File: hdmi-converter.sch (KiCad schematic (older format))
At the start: 127 parts, among them J2 46756-1001, Q1 BSS138APW, Q2 BSS138APW, Q3 BSS138APW, Q4 BSS138APW, U2 LT9611, U3 TXB0104RUT, U4 NTS0102GT, Y2 ABM8G-24.000MHZ-18-D2Y-T

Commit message: Cleanup
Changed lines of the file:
@@
 $Descr A3 16535 11693
 encoding utf-8
-Sheet 3 13
+Sheet 3 12
 Title ""
 Date ""
@@
 	1    0    0    -1
 $EndComp
-Text GLabel 1375 5425 0    50   Input ~ 0
+Text GLabel 1175 5425 0    50   Input ~ 0
 DSI1_LN3_N
-Text GLabel 1375 5525 0    50   Input ~ 0
+Text GLabel 1175 5525 0    50   Input ~ 0
 DSI1_LN3_P
-Text GLabel 1375 5625 0    50   Input ~ 0
+Text GLabel 1175 5625 0    50   Input ~ 0
 DSI1_LN2_N
-Text GLabel 1375 5725 0    50   Input ~ 0
+Text GLabel 1175 5725 0    50   Input ~ 0
 DSI1_LN2_P
-Text GLabel 1375 5825 0    50   Input ~ 0
+Text GLabel 1175 5825 0    50   Input ~ 0
 DSI1_CLK_N
-Text GLabel 1375 5925 0    50   Input ~ 0
+Text GLabel 1175 5925 0    50   Input ~ 0
 DSI1_CLK_P
-Text GLabel 1375 6025 0    50   Input ~ 0
+Text GLabel 1175 6025 0    50   Input ~ 0
 DSI1_LN1_N
-Text GLabel 1375 6125 0    50   Input ~ 0
+Text GLabel 1175 6125 0    50   Input ~ 0
 DSI1_LN1_P
-Text GLabel 1375 6225 0    50   Input ~ 0
+Text GLabel 1175 6225 0    50   Input ~ 0
 DSI1_LN0_N
 $Comp
@@
 	1700 10500 1550 10500
 Wire Wire Line
-	2500 10500 2650 10500
+	2500 10500 3350 10500
 Wire Wire Line
-	2500 10100 2650 10100
+	2500 10100 3350 10100
 Wire Wire Line
-	2500 10300 2650 10300
+	2500 10300 3350 10300
 Wire Wire Line
-	2500 9900 2650 9900
+	2500 9900 3350 9900
 Wire Wire Line
 	2000 9400 2000 9500
@@
 Connection ~ 1425 5225
 Wire Wire Line
-	1425 5225 1375 5225
+	1425 5225 675  5225
 Text GLabel 925  775  0    50   Input ~ 0
 3V3_SYS
@@
 $EndComp
 Wire Wire Line
-	8875 7950 12425 7950
+	8550 7950 12425 7950
 $Comp
 L sa800u-baseboard-hw:GND #PWR036
@@
 Connection ~ 2025 5025
 Wire Wire Line
-	1375 5125 1725 5125
+	675  5125 1725 5125
 Wire Wire Line
 	1425 4425 1725 4425
 Wire Wire Line
-	1375 5025 2025 5025
+	675  5025 2025 5025
 Wire Wire Line
 	1725 4425 2025 4425
@@
 Text Label 7175 8075 2    50   ~ 0
 VCOM
-Text Label 8875 6400 0    50   ~ 0
+Text Label 8550 6400 0    50   ~ 0
 HDMI_TX_D2_P
-Text Label 8875 6500 0    50   ~ 0
+Text Label 8550 6500 0    50   ~ 0
 HDMI_TX_D2_N
-Text Label 8875 6800 0    50   ~ 0
+Text Label 8550 6800 0    50   ~ 0
 HDMI_TX_D1_N
-Text Label 8875 7100 0    50   ~ 0
+Text Label 8550 7100 0    50   ~ 0
 HDMI_TX_D0_N
-Text Label 8875 7400 0    50   ~ 0
+Text Label 8550 7400 0    50   ~ 0
 HDMI_TX_CLK_N
-Text Label 8875 6700 0    50   ~ 0
+Text Label 8550 6700 0    50   ~ 0
 HDMI_TX_D1_P
-Text Label 8875 7000 0    50   ~ 0
+Text Label 8550 7000 0    50   ~ 0
 HDMI_TX_D0_P
-Text Label 8875 7300 0    50   ~ 0
+Text Label 8550 7300 0    50   ~ 0
 HDMI_TX_CLK_P
-Text Label 6350 10175 2    50   ~ 0
+Text Label 6050 10175 0    50   ~ 0
 LT9611_CEC
 Wire Wire Line
-	8875 6400 11375 6400
+	8550 6400 11375 6400
 Wire Wire Line
-	8875 6500 11075 6500
+	8550 6500 11075 6500
 Wire Wire Line
-	8875 7000 10175 7000
+	8550 7000 10175 7000
 Wire Wire Line
-	8875 7100 9875 7100
+	8550 7100 9875 7100
 Wire Wire Line
-	8875 7400 9275 7400
+	8550 7400 9275 7400
 Wire Wire Line
-	8875 7300 9575 7300
+	8550 7300 9575 7300
 Wire Wire Line
-	8875 6800 10475 6800
+	8550 6800 10475 6800
 Wire Wire Line
-	8875 6700 10775 6700
+	8550 6700 10775 6700
 Wire Wire Line
 	1700 9700 1650 9700
@@
 Wire Wire Line
 	3050 9100 3300 9100
-Text Label 1375 6525 2    50   ~ 0
+Text Label 700  6525 0    50   ~ 0
 LT9611_I2S_WS
-Text Label 1375 6625 2    50   ~ 0
+Text Label 700  6625 0    50   ~ 0
 LT9611_I2S_SCLK
-Text Label 1375 6725 2    50   ~ 0
+Text Label 700  6725 0    50   ~ 0
 LT9611_I2S_MCLK
-Text Label 1375 6825 2    50   ~ 0
+Text Label 700  6825 0    50   ~ 0
 LT9611_I2S_D0_SPDIF
-Text Label 2650 9900 0    50   ~ 0
+Text Label 3350 9900 2    50   ~ 0
 LT9611_I2S_WS
-Text Label 2650 10100 0    50   ~ 0
+Text Label 3350 10100 2    50   ~ 0
 LT9611_I2S_SCLK
-Text Label 2650 10300 0    50   ~ 0
+Text Label 3350 10300 2    50   ~ 0
 LT9611_I2S_MCLK
-Text Label 2650 10500 0    50   ~ 0
+Text Label 3350 10500 2    50   ~ 0
 LT9611_I2S_D0_SPDIF
 Wire Wire Line
@@
 Connection ~ 5300 9750
 Wire Wire Line
-	5300 9750 5500 9750
+	5300 9750 6025 9750
 Wire Wire Line
 	5250 10575 5300 10575
@@
 Wire Wire Line
 	5300 10575 5425 10575
-Text Label 1375 5225 2    50   ~ 0
+Text Label 675  5225 0    50   ~ 0
 LT9611_RST_N
-Text Label 1375 4925 2    50   ~ 0
+Text Label 675  4925 0    50   ~ 0
 LT9611_INTO_GPIO5
 Wire Wire Line
@@
 	6550 10175 6600 10175
 Wire Wire Line
-	6350 10175 6550 10175
+	6050 10175 6550 10175
 Text GLabel 6650 9325 0    50   Input ~ 0
 3V3_SYS
@@
 Connection ~ 7050 10175
 Wire Wire Line
-	7050 10175 7250 10175
-Text Label 7250 10175 0    50   ~ 0
+	7050 10175 7675 10175
+Text Label 7675 10175 2    50   ~ 0
 HDMI_CEC
 Wire Wire Line
@@
 Connection ~ 5425 10575
 Wire Wire Line
-	5425 10575 5500 10575
+	5425 10575 6025 10575
 Text Notes 5750 10900 0    50   ~ 0
 Note:\nplace close to\npin 17 of U2
 Wire Wire Line
-	1375 5425 3500 5425
+	1175 5425 3500 5425
 Wire Wire Line
-	1375 5525 3500 5525
+	1175 5525 3500 5525
 Wire Wire Line
-	1375 5625 3500 5625
+	1175 5625 3500 5625
 Wire Wire Line
-	1375 5725 3500 5725
+	1175 5725 3500 5725
 Wire Wire Line
-	1375 5825 3500 5825
+	1175 5825 3500 5825
 Wire Wire Line
-	1375 5925 3500 5925
+	1175 5925 3500 5925
 Wire Wire Line
-	1375 6025 3500 6025
+	1175 6025 3500 6025
 Wire Wire Line
-	1375 6125 3500 6125
+	1175 6125 3500 6125
 Wire Wire Line
-	1375 6225 3500 6225
+	1175 6225 3500 6225
 Wire Wire Line
-	1375 6325 3500 6325
+	1175 6325 3500 6325
 Wire Wire Line
-	1375 6525 3500 6525
+	700  6525 3500 6525
 Wire Wire Line
-	1375 6625 3500 6625
+	700  6625 3500 6625
 Wire Wire Line
-	1375 6725 3500 6725
+	700  6725 3500 6725
 Wire Wire Line
-	1375 6825 3500 6825
+	700  6825 3500 6825
 Wire Wire Line
 	1375 7875 3500 7875
@@
 	0    1    1    0
 $EndComp
-Text Label 1375 5025 2    50   ~ 0
+Text Label 675  5025 0    50   ~ 0
 LT9611_SCL
-Text Label 1375 5125 2    50   ~ 0
+Text Label 675  5125 0    50   ~ 0
 LT9611_SDA
-Text Label 8875 7950 0    50   ~ 0
+Text Label 8550 7950 0    50   ~ 0
 VCOM
 Text GLabel 1550 9400 0    50   Input ~ 0
@@
 Wire Wire Line
 	4800 4925 5625 4925
-Text GLabel 1375 6325 0    50   Input ~ 0
+Text GLabel 1175 6325 0    50   Input ~ 0
 DSI1_LN0_P
 $Comp
@@
 Wire Wire Line
 	11625 2225 11625 3425
-Text Label 5500 10575 0    50   ~ 0
+Text Label 6025 10575 2    50   ~ 0
 LT9611_RST_N
-Text Label 5500 9750 0    50   ~ 0
+Text Label 6025 9750 2    50   ~ 0
 LT9611_INTO_GPIO5
 $Comp
@@
 	2025 5275 2025 5025
 Wire Wire Line
-	1375 4925 2350 4925
+	675  4925 2350 4925
 Wire Wire Line
 	2350 5275 2350 4925

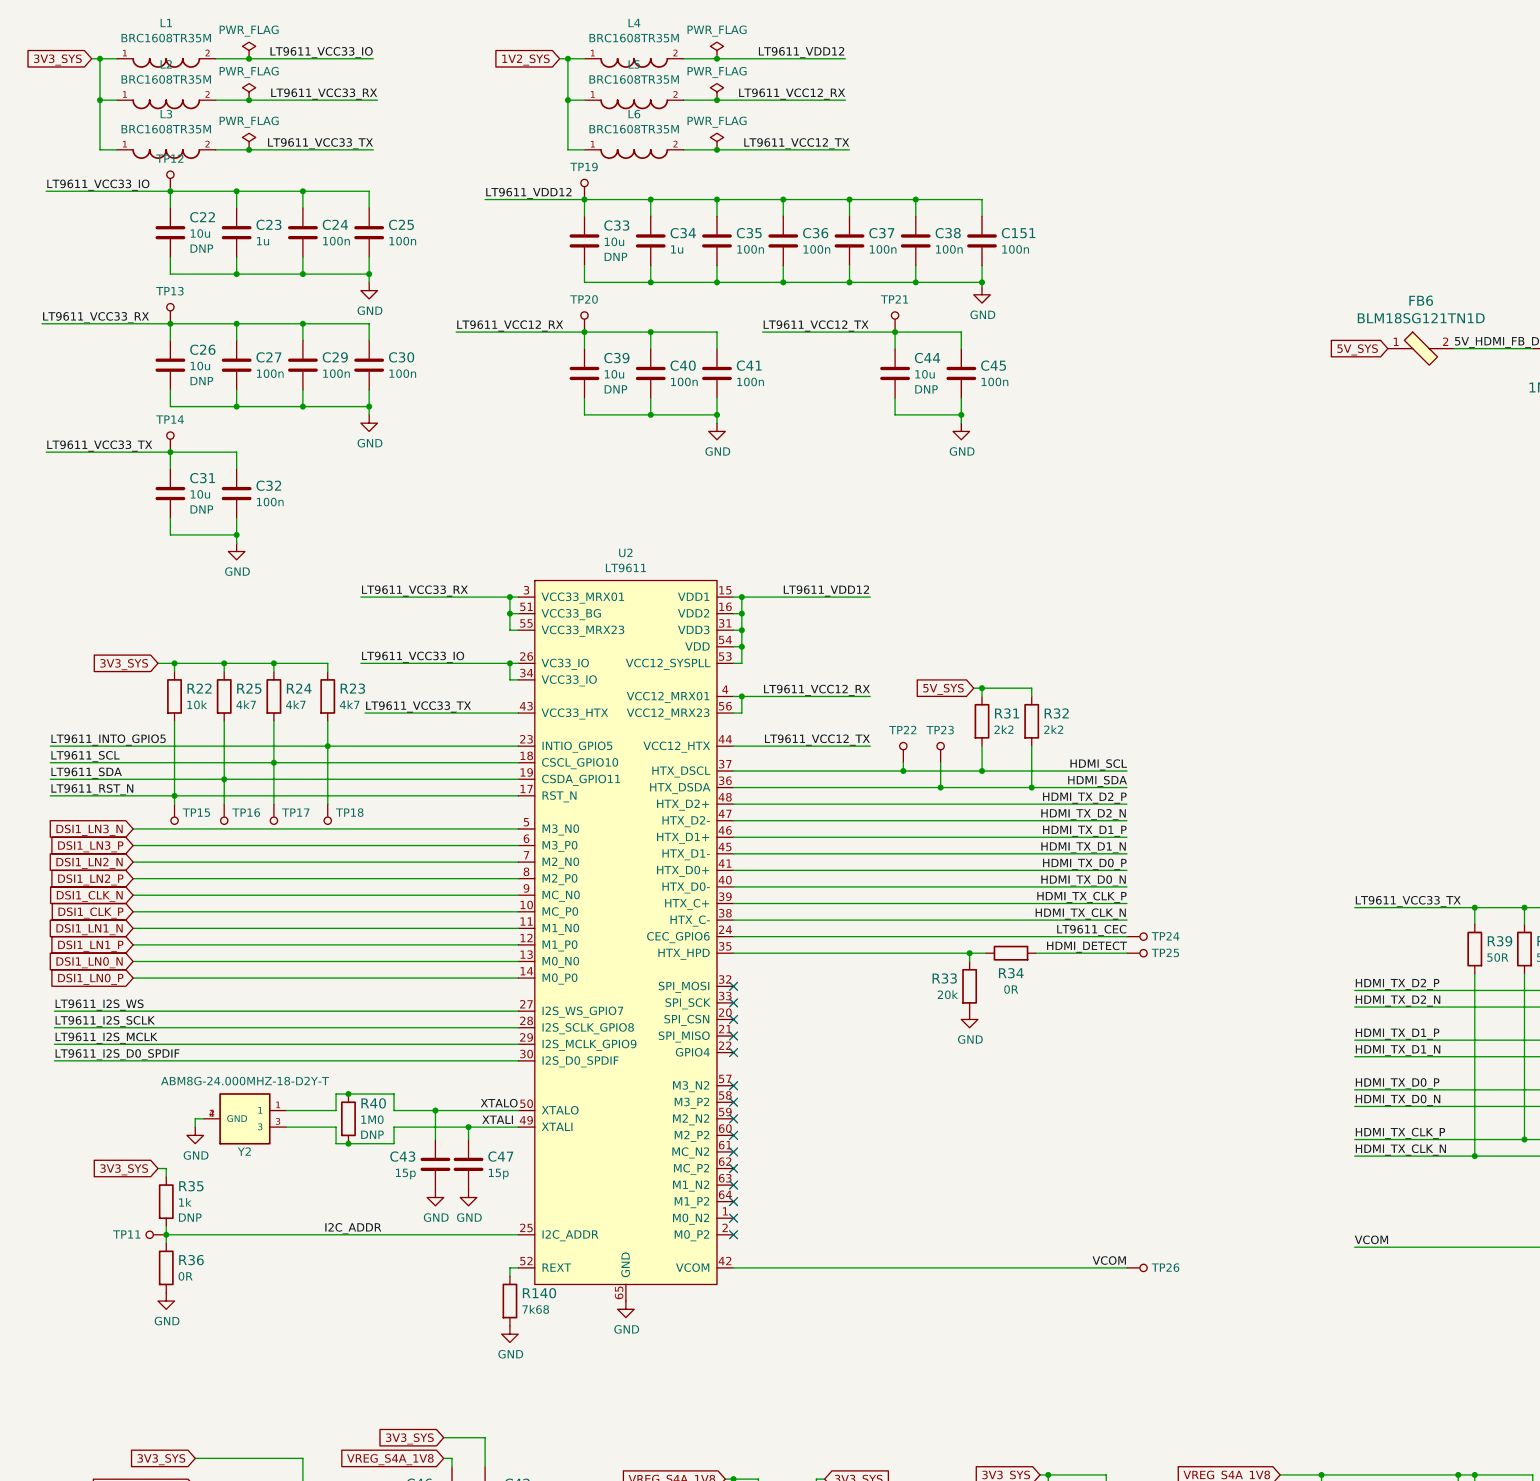
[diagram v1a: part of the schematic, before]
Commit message: Reorganize schematics, add descriptions in top left corner
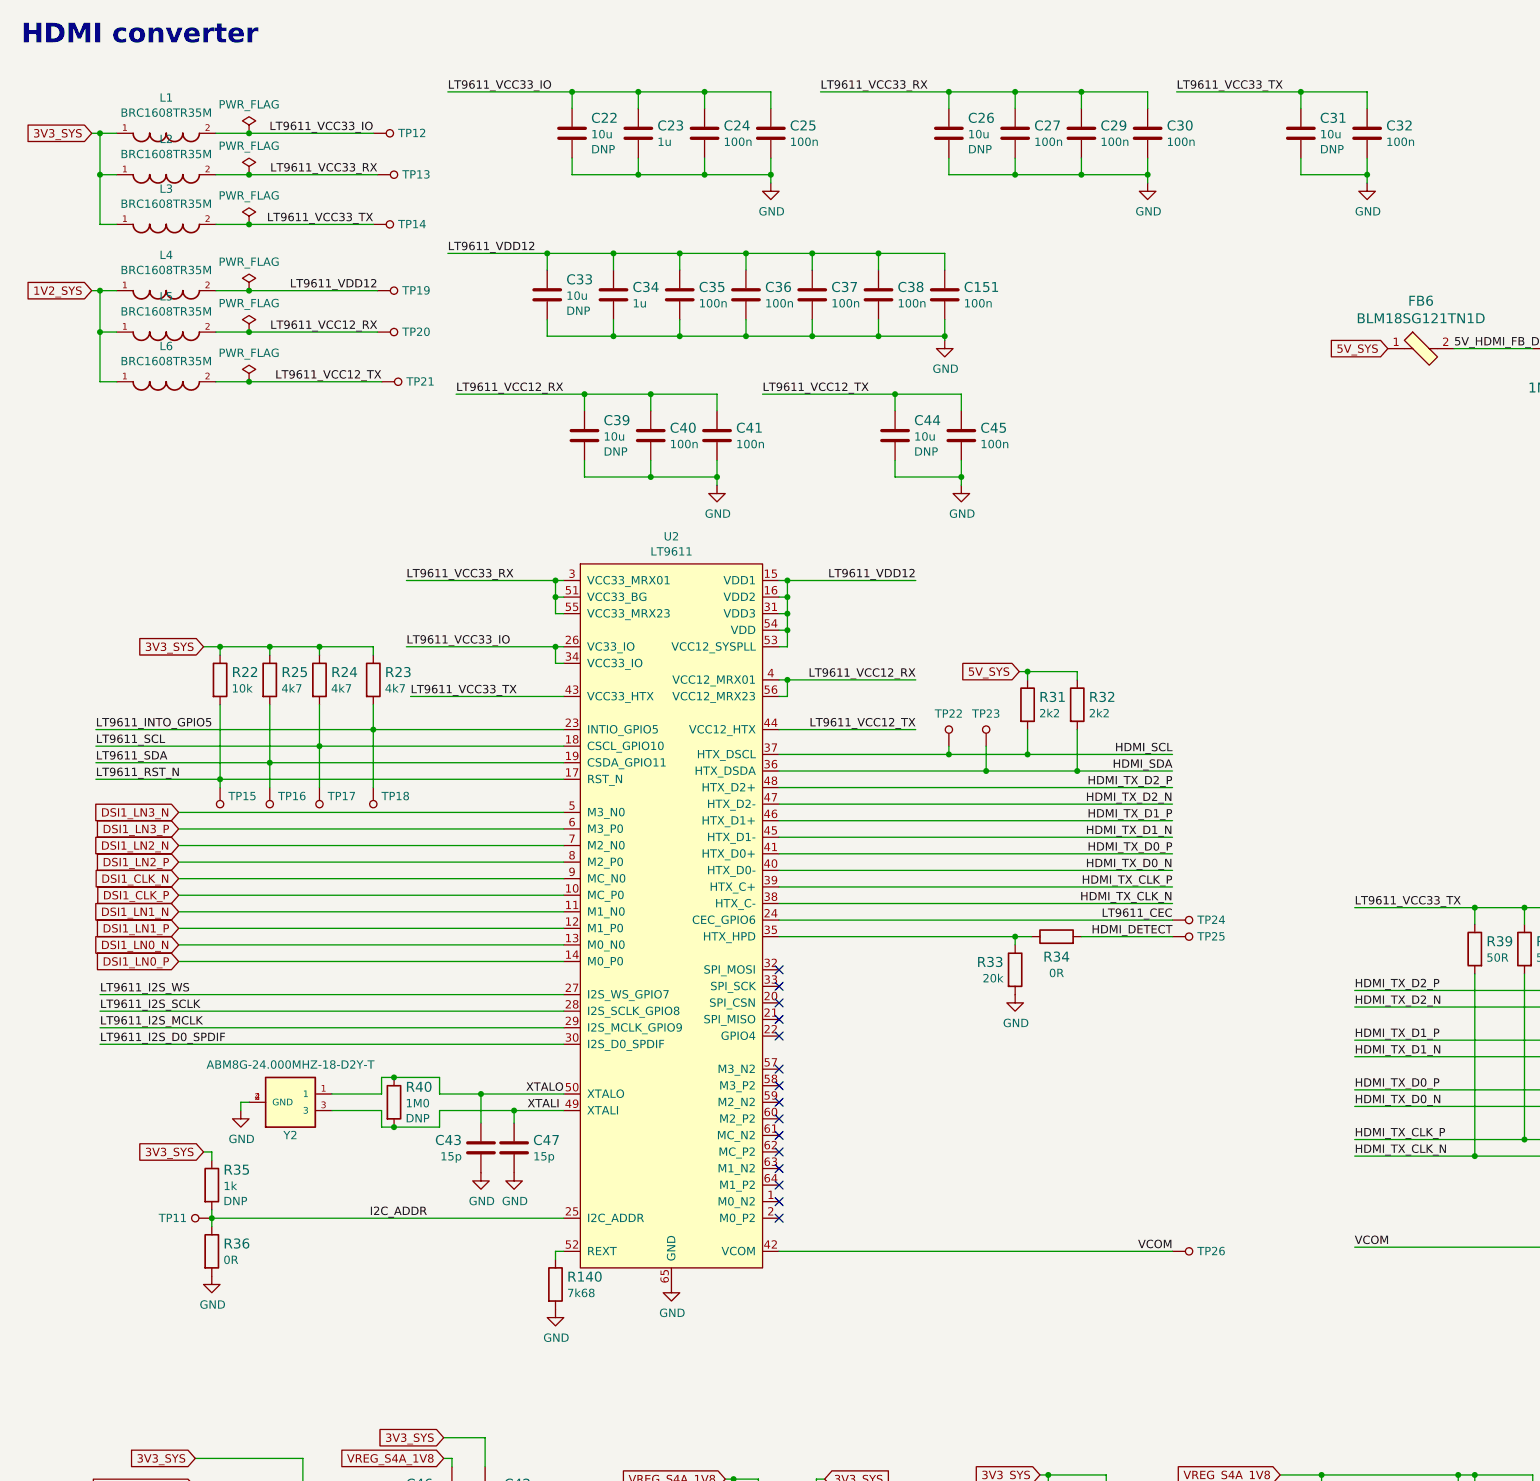
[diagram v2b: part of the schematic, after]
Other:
- note added: "HDMI converter"
- moved on the sheet: C151, C22, C23, C24, C25, C26, C27, C29, C30, C31, C32, C33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

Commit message: Add testpoints to PCB, udpate cache, connect STUSB4500 reset to SoM and pulldown with 10k
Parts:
- removed TP16, TP17: TP_SMD_0_75MM, sa800u-baseboard-hw-footprints:Testpoint_smd_0_75mm, symbol sa800u-baseboard-hw:TP_SMD_0_75MM
- added TP16: TP, antmicro-footprints:TP-R-1.5, symbol antmicroTestPoints:TP
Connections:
- net GND: now also TP16.1
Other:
- moved on the sheet: TP15, TP18
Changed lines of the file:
@@
 L sa800u-baseboard-hw:TP_SMD_0_75MM TP?
 U 1 1 6297FFC8
-P 1700 5275
+P 6125 10575
 AR Path="/618E716E/6297FFC8" Ref="TP?"  Part="1"
 AR Path="/6197686D/6297FFC8" Ref="TP15"  Part="1"
-F 0 "TP15" H 1750 5322 50  0000 L CNN
-F 1 "TP_SMD_0_75MM" H 1700 5175 50  0001 C CNN
-F 2 "sa800u-baseboard-hw-footprints:Testpoint_smd_0_75mm" H 1900 5475 60  0001 L CNN
-F 3 "" H 1900 5575 60  0001 L CNN
-	1    1700 5275
-	1    0    0    -1
-$EndComp
-$Comp
-L sa800u-baseboard-hw:TP_SMD_0_75MM TP?
-U 1 1 62A0D2B6
-P 2000 5275
-AR Path="/618E716E/62A0D2B6" Ref="TP?"  Part="1"
-AR Path="/6197686D/62A0D2B6" Ref="TP16"  Part="1"
-F 0 "TP16" H 2050 5322 50  0000 L CNN
-F 1 "TP_SMD_0_75MM" H 2000 5175 50  0001 C CNN
-F 2 "sa800u-baseboard-hw-footprints:Testpoint_smd_0_75mm" H 2200 5475 60  0001 L CNN
-F 3 "" H 2200 5575 60  0001 L CNN
-	1    2000 5275
-	1    0    0    -1
-$EndComp
-$Comp
-L sa800u-baseboard-hw:TP_SMD_0_75MM TP?
-U 1 1 62A99631
-P 2300 5275
-AR Path="/618E716E/62A99631" Ref="TP?"  Part="1"
-AR Path="/6197686D/62A99631" Ref="TP17"  Part="1"
-F 0 "TP17" H 2350 5322 50  0000 L CNN
-F 1 "TP_SMD_0_75MM" H 2300 5175 50  0001 C CNN
-F 2 "sa800u-baseboard-hw-footprints:Testpoint_smd_0_75mm" H 2500 5475 60  0001 L CNN
-F 3 "" H 2500 5575 60  0001 L CNN
-	1    2300 5275
-	1    0    0    -1
-$EndComp
-$Comp
-L sa800u-baseboard-hw:TP_SMD_0_75MM TP?
-U 1 1 62AE01B3
-P 2625 5275
-AR Path="/618E716E/62AE01B3" Ref="TP?"  Part="1"
-AR Path="/6197686D/62AE01B3" Ref="TP18"  Part="1"
-F 0 "TP18" H 2675 5322 50  0000 L CNN
-F 1 "TP_SMD_0_75MM" H 2625 5175 50  0001 C CNN
-F 2 "sa800u-baseboard-hw-footprints:Testpoint_smd_0_75mm" H 2825 5475 60  0001 L CNN
-F 3 "" H 2825 5575 60  0001 L CNN
-	1    2625 5275
-	1    0    0    -1
-$EndComp
-Wire Wire Line
-	1700 5175 1700 5125
-Wire Wire Line
-	2000 5175 2000 5025
-Wire Wire Line
-	2300 5175 2300 4925
+F 0 "TP15" V 6125 10525 50  0000 R CNN
+F 1 "TP_SMD_0_75MM" H 6125 10475 50  0001 C CNN
+F 2 "sa800u-baseboard-hw-footprints:Testpoint_smd_0_75mm" H 6325 10775 60  0001 L CNN
+F 3 "" H 6325 10875 60  0001 L CNN
+	1    6125 10575
+	0    -1   -1   0
+$EndComp
 Wire Wire Line
 	950  4825 2625 4825
-Wire Wire Line
-	2625 5175 2625 4825
 $Comp
 L sa800u-baseboard-hw:TP_SMD_0_75MM TP?
@@
 	4625 1475 5025 1475
 Connection ~ 4625 1475
+$Comp
+L sa800u-baseboard-hw:TP_SMD_0_75MM TP?
+U 1 1 62AE01B3
+P 6125 9750
+AR Path="/618E716E/62AE01B3" Ref="TP?"  Part="1"
+AR Path="/6197686D/62AE01B3" Ref="TP18"  Part="1"
+F 0 "TP18" V 6125 9700 50  0000 R CNN
+F 1 "TP_SMD_0_75MM" H 6125 9650 50  0001 C CNN
+F 2 "sa800u-baseboard-hw-footprints:Testpoint_smd_0_75mm" H 6325 9950 60  0001 L CNN
+F 3 "" H 6325 10050 60  0001 L CNN
+	1    6125 9750
+	0    -1   -1   0
+$EndComp
+$Comp
+L antmicroTestPoints:TP TP?
+U 1 1 68F4B7A6
+P 15825 9600
+AR Path="/61A19323/68F4B7A6" Ref="TP?"  Part="1"
+AR Path="/6197686D/68F4B7A6" Ref="TP16"  Part="1"
+F 0 "TP16" H 15737 9647 50  0000 R CNN
+F 1 "TP" H 15825 9600 50  0001 C CNN
+F 2 "antmicro-footprints:TP-R-1.5" H 15825 9600 50  0001 C CNN
+F 3 "" H 15825 9600 50  0001 C CNN
+	1    15825 9600
+	-1   0    0    1
+$EndComp
+$Comp
+L sa800u-baseboard-hw:GND #PWR?
+U 1 1 68FDECE8
+P 15825 9700
+AR Path="/61BD2CC1/68FDECE8" Ref="#PWR?"  Part="1"
+AR Path="/6197686D/68FDECE8" Ref="#PWR0279"  Part="1"
+F 0 "#PWR0279" H 15825 9450 50  0001 C CNN
+F 1 "GND" H 15830 9527 50  0000 C CNN
+F 2 "" H 15825 9700 50  0001 C CNN
+F 3 "" H 15825 9700 50  0001 C CNN
+	1    15825 9700
+	1    0    0    -1
+$EndComp
 $EndSCHEMATC

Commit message: Clear annotation and annotate
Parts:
- renumbered C46 to C18, C43 to C19, C42 to C20, C47 to C21, C33 to C22, C22 to C23, C39 to C24, C34 to C25, C23 to C26, C40 to C27, C35 to C28, C24 to C29, C41 to C30, C36 to C31, C25 to C32, C37 to C33, C28 to C34, C38 to C35, C44 to C36, C151 to C37, C26 to C38, C45 to C39, C27 to C40, C29 to C41, C30 to C42, C31 to C43, C97 to C44, C32 to C45, C50 to C46, C52 to C47, C54 to C48, C56 to C49, C49 to C50, C53 to C52, C55 to C53, C98 to C54, C57 to C55, C58 to C56, C59 to C57, D3 to D1, D7 to D2, D4 to D3, D5 to D4, D6 to D5, FB6 to FB2, R35 to R15, R36 to R16, R22 to R17, R25 to R18, R24 to R19, R23 to R20, R40 to R21, R140 to R22, R26 to R23, R27 to R24, R29 to R25, R30 to R26, R33 to R27, R31 to R28, R19 to R29, R34 to R30, R20 to R31, R21 to R33, R37 to R34, R39 to R35, R38 to R36, R41 to R37, R42 to R38, R43 to R39, R44 to R40, R53 to R41, R45 to R42, R55 to R43, R47 to R44, R46 to R45, R48 to R46, R51 to R47, R143 to R48, R58 to R49, R59 to R50, R60 to R51, R61 to R52, R62 to R53, R87 to R54, R134 to R55, R137 to R56, TP12 to TP10, TP14 to TP11, TP13 to TP12, TP19 to TP13, TP20 to TP14, TP21 to TP15, TP22 to TP16, TP18 to TP17, TP15 to TP18, TP23 to TP19, TP24 to TP20, TP25 to TP21, TP26 to TP22, TP27 to TP23, TP28 to TP24, TP29 to TP25, TP30 to TP26, TP16 to TP27, TP11 to TP9, U3 to U2, U2 to U3

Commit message: Loclib after anotation
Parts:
- TP27: footprint antmicro-footprints:TP-R-1.5 -> sa800u-baseboard-hw-footprints:TP-R-1.5; symbol antmicroTestPoints:TP -> sa800u-baseboard-hw:TP
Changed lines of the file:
@@
 $EndComp
 $Comp
-L antmicroTestPoints:TP TP?
+L sa800u-baseboard-hw:TP TP?
 U 1 1 68F4B7A6
 P 15825 9600
@@
 F 0 "TP27" H 15737 9647 50  0000 R CNN
 F 1 "TP" H 15825 9600 50  0001 C CNN
-F 2 "antmicro-footprints:TP-R-1.5" H 15825 9600 50  0001 C CNN
+F 2 "sa800u-baseboard-hw-footprints:TP-R-1.5" H 15825 9600 50  0001 C CNN
 F 3 "" H 15825 9600 50  0001 C CNN
 	1    15825 9600
